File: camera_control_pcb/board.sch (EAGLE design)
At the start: 17 parts, among them Q1 MPSA42

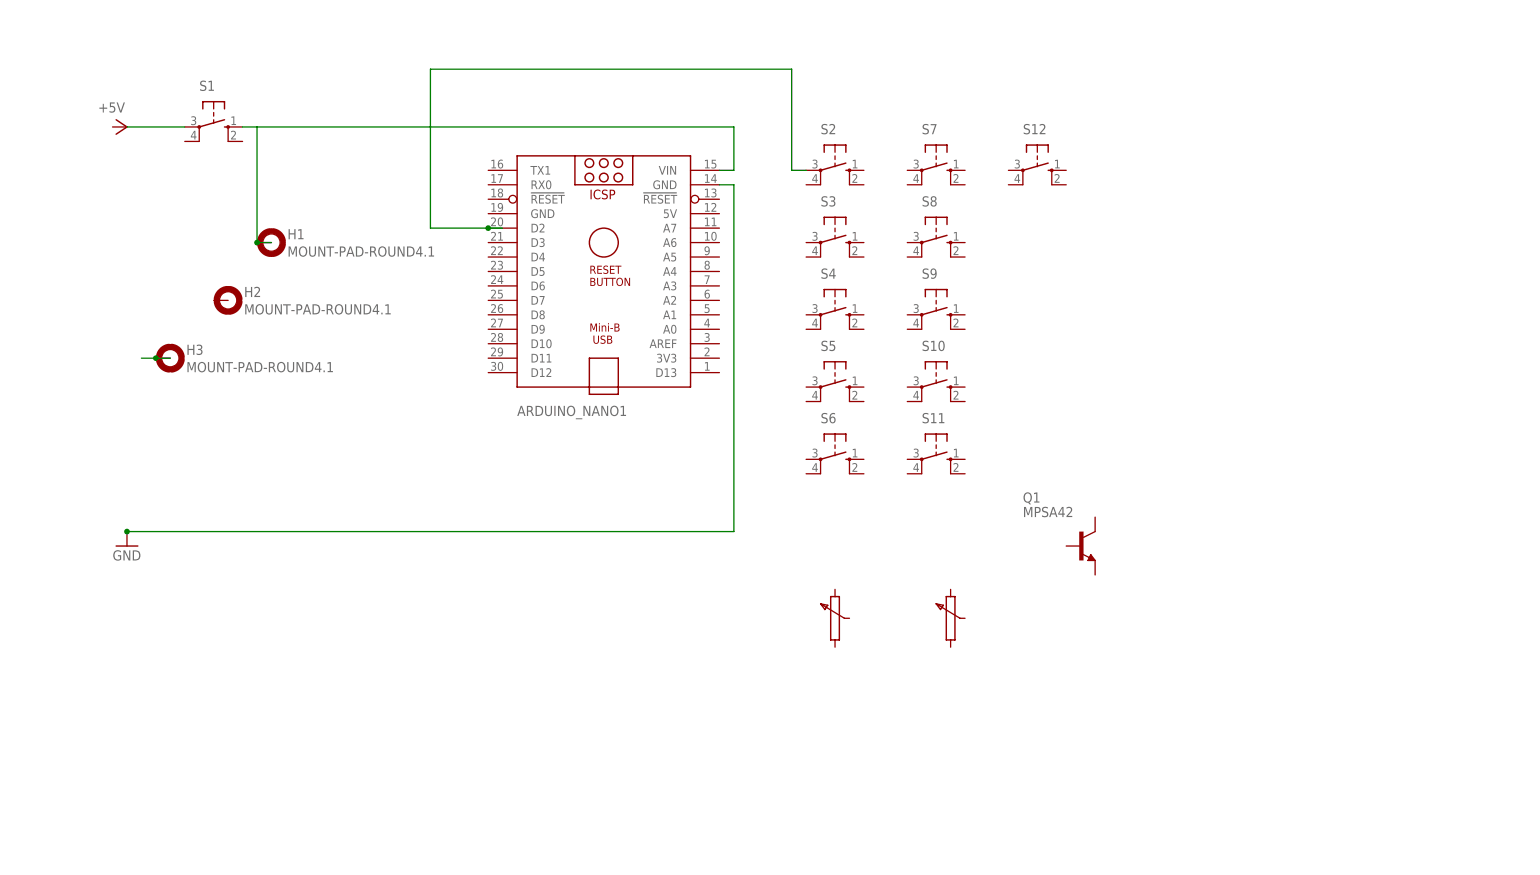
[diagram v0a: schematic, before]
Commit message: Rest of switch pins; demo board layout
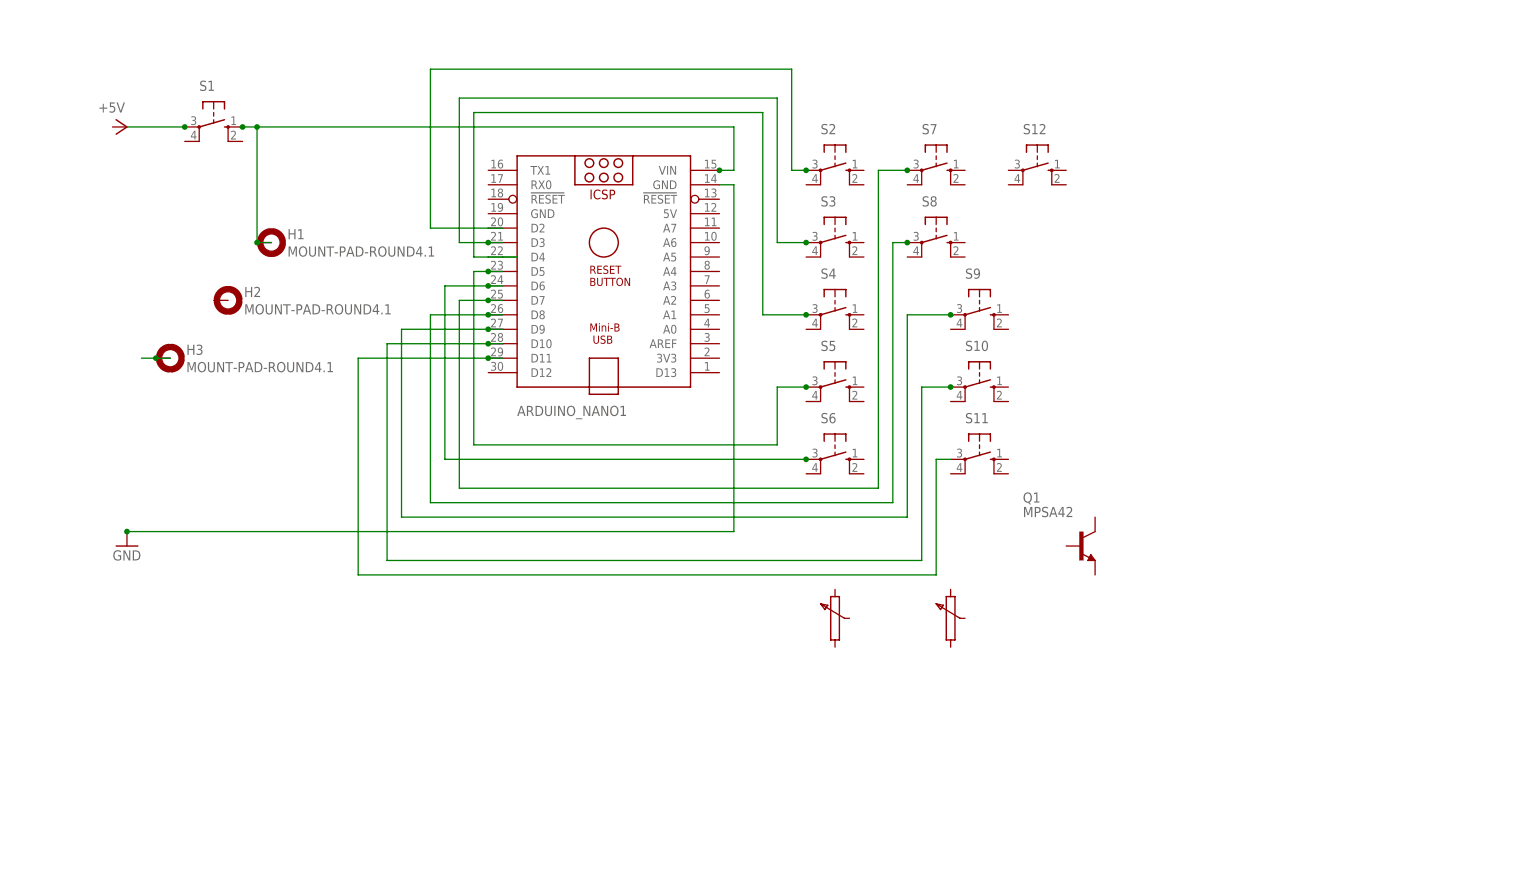
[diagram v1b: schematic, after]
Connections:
- new net N$10: ARDUINO_NANO1.D9, S9.P
- new net N$11: ARDUINO_NANO1.D10, S10.P
- new net N$12: ARDUINO_NANO1.D11, S11.P
- new net N$14: ARDUINO_NANO1.D4, S4.P
- new net N$5: ARDUINO_NANO1.D3, S3.P
- new net N$6: ARDUINO_NANO1.D7, S7.P
- new net N$7: ARDUINO_NANO1.D5, S5.P
- new net N$8: ARDUINO_NANO1.D6, S6.P
- new net N$9: ARDUINO_NANO1.D8, S8.P
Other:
- moved on the sheet: S10, S11, S9
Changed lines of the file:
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@@
 <attribute name="VALUE" x="104.775" y="72.39" size="1.778" layer="96"/>
 </instance>
-<instance part="S9" gate="1" x="101.6" y="55.88" smashed="yes" rot="R270">
-<attribute name="NAME" x="99.06" y="62.23" size="1.778" layer="95"/>
-<attribute name="VALUE" x="104.775" y="59.69" size="1.778" layer="96"/>
-</instance>
-<instance part="S10" gate="1" x="101.6" y="43.18" smashed="yes" rot="R270">
-<attribute name="NAME" x="99.06" y="49.53" size="1.778" layer="95"/>
-<attribute name="VALUE" x="104.775" y="46.99" size="1.778" layer="96"/>
-</instance>
-<instance part="S11" gate="1" x="101.6" y="30.48" smashed="yes" rot="R270">
-<attribute name="NAME" x="99.06" y="36.83" size="1.778" layer="95"/>
-<attribute name="VALUE" x="104.775" y="34.29" size="1.778" layer="96"/>
+<instance part="S9" gate="1" x="109.22" y="55.88" smashed="yes" rot="R270">
+<attribute name="NAME" x="106.68" y="62.23" size="1.778" layer="95"/>
+<attribute name="VALUE" x="112.395" y="59.69" size="1.778" layer="96"/>
+</instance>
+<instance part="S10" gate="1" x="109.22" y="43.18" smashed="yes" rot="R270">
+<attribute name="NAME" x="106.68" y="49.53" size="1.778" layer="95"/>
+<attribute name="VALUE" x="112.395" y="46.99" size="1.778" layer="96"/>
+</instance>
+<instance part="S11" gate="1" x="109.22" y="30.48" smashed="yes" rot="R270">
+<attribute name="NAME" x="106.68" y="36.83" size="1.778" layer="95"/>
+<attribute name="VALUE" x="112.395" y="34.29" size="1.778" layer="96"/>
 </instance>
 <instance part="S12" gate="1" x="119.38" y="81.28" smashed="yes" rot="R270">
@@
 <pinref part="S1" gate="1" pin="P"/>
 <wire x1="-40.64" y1="88.9" x2="-30.48" y2="88.9" width="0.1524" layer="91"/>
+<junction x="-30.48" y="88.9"/>
 </segment>
 </net>
@@
 <pinref part="H1" gate="G$1" pin="MOUNT"/>
 <junction x="-17.78" y="68.58"/>
+<junction x="-17.78" y="88.9"/>
+<junction x="63.5" y="81.28"/>
+<junction x="-20.32" y="88.9"/>
 </segment>
 </net>
@@
 <net name="N$5" class="0">
 <segment>
+<wire x1="25.4" y1="68.58" x2="22.86" y2="68.58" width="0.1524" layer="91"/>
+<wire x1="22.86" y1="68.58" x2="17.78" y2="68.58" width="0.1524" layer="91"/>
+<wire x1="17.78" y1="68.58" x2="17.78" y2="93.98" width="0.1524" layer="91"/>
+<wire x1="17.78" y1="93.98" x2="73.66" y2="93.98" width="0.1524" layer="91"/>
+<wire x1="73.66" y1="93.98" x2="73.66" y2="68.58" width="0.1524" layer="91"/>
+<pinref part="S3" gate="1" pin="P"/>
+<wire x1="73.66" y1="68.58" x2="78.74" y2="68.58" width="0.1524" layer="91"/>
+<pinref part="ARDUINO_NANO1" gate="G$1" pin="D3"/>
+<junction x="22.86" y="68.58"/>
+<junction x="78.74" y="68.58"/>
+</segment>
+</net>
+<net name="N$7" class="0">
+<segment>
+<pinref part="S5" gate="1" pin="P"/>
+<wire x1="78.74" y1="43.18" x2="73.66" y2="43.18" width="0.1524" layer="91"/>
+<wire x1="73.66" y1="43.18" x2="73.66" y2="33.02" width="0.1524" layer="91"/>
+<wire x1="73.66" y1="33.02" x2="20.32" y2="33.02" width="0.1524" layer="91"/>
+<wire x1="20.32" y1="33.02" x2="20.32" y2="63.5" width="0.1524" layer="91"/>
+<wire x1="20.32" y1="63.5" x2="22.86" y2="63.5" width="0.1524" layer="91"/>
+<pinref part="ARDUINO_NANO1" gate="G$1" pin="D5"/>
+<wire x1="22.86" y1="63.5" x2="25.4" y2="63.5" width="0.1524" layer="91"/>
+<junction x="22.86" y="63.5"/>
+<junction x="78.74" y="43.18"/>
+</segment>
+</net>
+<net name="N$8" class="0">
+<segment>
+<pinref part="S6" gate="1" pin="P"/>
+<wire x1="78.74" y1="30.48" x2="15.24" y2="30.48" width="0.1524" layer="91"/>
+<wire x1="15.24" y1="30.48" x2="15.24" y2="60.96" width="0.1524" layer="91"/>
+<wire x1="15.24" y1="60.96" x2="22.86" y2="60.96" width="0.1524" layer="91"/>
+<pinref part="ARDUINO_NANO1" gate="G$1" pin="D6"/>
+<wire x1="22.86" y1="60.96" x2="25.4" y2="60.96" width="0.1524" layer="91"/>
+<junction x="22.86" y="60.96"/>
+<junction x="78.74" y="30.48"/>
+</segment>
+</net>
+<net name="N$6" class="0">
+<segment>
+<pinref part="S7" gate="1" pin="P"/>
+<wire x1="96.52" y1="81.28" x2="91.44" y2="81.28" width="0.1524" layer="91"/>
+<wire x1="91.44" y1="81.28" x2="91.44" y2="25.4" width="0.1524" layer="91"/>
+<wire x1="91.44" y1="25.4" x2="17.78" y2="25.4" width="0.1524" layer="91"/>
+<wire x1="17.78" y1="25.4" x2="17.78" y2="58.42" width="0.1524" layer="91"/>
+<wire x1="17.78" y1="58.42" x2="22.86" y2="58.42" width="0.1524" layer="91"/>
+<pinref part="ARDUINO_NANO1" gate="G$1" pin="D7"/>
+<wire x1="22.86" y1="58.42" x2="25.4" y2="58.42" width="0.1524" layer="91"/>
+<junction x="22.86" y="58.42"/>
+<junction x="96.52" y="81.28"/>
+</segment>
+</net>
+<net name="N$9" class="0">
+<segment>
+<pinref part="S8" gate="1" pin="P"/>
+<wire x1="96.52" y1="68.58" x2="93.98" y2="68.58" width="0.1524" layer="91"/>
+<wire x1="93.98" y1="68.58" x2="93.98" y2="22.86" width="0.1524" layer="91"/>
+<wire x1="93.98" y1="22.86" x2="12.7" y2="22.86" width="0.1524" layer="91"/>
+<wire x1="12.7" y1="22.86" x2="12.7" y2="55.88" width="0.1524" layer="91"/>
+<wire x1="12.7" y1="55.88" x2="22.86" y2="55.88" width="0.1524" layer="91"/>
+<pinref part="ARDUINO_NANO1" gate="G$1" pin="D8"/>
+<wire x1="22.86" y1="55.88" x2="25.4" y2="55.88" width="0.1524" layer="91"/>
+<junction x="22.86" y="55.88"/>
+<junction x="96.52" y="68.58"/>
+</segment>
+</net>
+<net name="N$10" class="0">
+<segment>
+<pinref part="S9" gate="1" pin="P"/>
+<wire x1="104.14" y1="55.88" x2="96.52" y2="55.88" width="0.1524" layer="91"/>
+<wire x1="96.52" y1="55.88" x2="96.52" y2="20.32" width="0.1524" layer="91"/>
+<wire x1="96.52" y1="20.32" x2="7.62" y2="20.32" width="0.1524" layer="91"/>
+<wire x1="7.62" y1="20.32" x2="7.62" y2="53.34" width="0.1524" layer="91"/>
+<wire x1="7.62" y1="53.34" x2="22.86" y2="53.34" width="0.1524" layer="91"/>
+<pinref part="ARDUINO_NANO1" gate="G$1" pin="D9"/>
+<junction x="22.86" y="53.34"/>
+<wire x1="22.86" y1="53.34" x2="25.4" y2="53.34" width="0.1524" layer="91"/>
+<junction x="104.14" y="55.88"/>
+</segment>
+</net>
+<net name="N$11" class="0">
+<segment>
+<pinref part="S10" gate="1" pin="P"/>
+<wire x1="104.14" y1="43.18" x2="99.06" y2="43.18" width="0.1524" layer="91"/>
+<wire x1="99.06" y1="43.18" x2="99.06" y2="12.7" width="0.1524" layer="91"/>
+<wire x1="99.06" y1="12.7" x2="5.08" y2="12.7" width="0.1524" layer="91"/>
+<wire x1="5.08" y1="12.7" x2="5.08" y2="50.8" width="0.1524" layer="91"/>
+<wire x1="5.08" y1="50.8" x2="22.86" y2="50.8" width="0.1524" layer="91"/>
+<pinref part="ARDUINO_NANO1" gate="G$1" pin="D10"/>
+<junction x="22.86" y="50.8"/>
+<wire x1="22.86" y1="50.8" x2="25.4" y2="50.8" width="0.1524" layer="91"/>
+<junction x="104.14" y="43.18"/>
+</segment>
+</net>
+<net name="N$12" class="0">
+<segment>
+<pinref part="S11" gate="1" pin="P"/>
+<wire x1="104.14" y1="30.48" x2="101.6" y2="30.48" width="0.1524" layer="91"/>
+<wire x1="101.6" y1="30.48" x2="101.6" y2="10.16" width="0.1524" layer="91"/>
+<wire x1="101.6" y1="10.16" x2="0" y2="10.16" width="0.1524" layer="91"/>
+<wire x1="0" y1="10.16" x2="0" y2="48.26" width="0.1524" layer="91"/>
+<wire x1="0" y1="48.26" x2="22.86" y2="48.26" width="0.1524" layer="91"/>
+<pinref part="ARDUINO_NANO1" gate="G$1" pin="D11"/>
+<junction x="22.86" y="48.26"/>
+<wire x1="22.86" y1="48.26" x2="25.4" y2="48.26" width="0.1524" layer="91"/>
+</segment>
+</net>
+<net name="N$13" class="0">
+<segment>
+<pinref part="S2" gate="1" pin="P"/>
+<junction x="78.74" y="81.28"/>
+<wire x1="76.2" y1="81.28" x2="78.74" y2="81.28" width="0.1524" layer="91"/>
+<wire x1="76.2" y1="99.06" x2="76.2" y2="81.28" width="0.1524" layer="91"/>
+<wire x1="12.7" y1="99.06" x2="76.2" y2="99.06" width="0.1524" layer="91"/>
+<wire x1="12.7" y1="71.12" x2="12.7" y2="99.06" width="0.1524" layer="91"/>
 <wire x1="25.4" y1="71.12" x2="22.86" y2="71.12" width="0.1524" layer="91"/>
-<wire x1="22.86" y1="71.12" x2="12.7" y2="71.12" width="0.1524" layer="91"/>
-<wire x1="12.7" y1="71.12" x2="12.7" y2="99.06" width="0.1524" layer="91"/>
-<wire x1="12.7" y1="99.06" x2="76.2" y2="99.06" width="0.1524" layer="91"/>
-<pinref part="S2" gate="1" pin="P"/>
-<wire x1="76.2" y1="99.06" x2="76.2" y2="81.28" width="0.1524" layer="91"/>
-<wire x1="76.2" y1="81.28" x2="78.74" y2="81.28" width="0.1524" layer="91"/>
 <pinref part="ARDUINO_NANO1" gate="G$1" pin="D2"/>
-<junction x="22.86" y="71.12"/>
-</segment>
-</net>
+<wire x1="12.7" y1="71.12" x2="22.86" y2="71.12" width="0.1524" layer="91"/>
+</segment>
+</net>
+<net name="N$14" class="0">
+<segment>
+<pinref part="S4" gate="1" pin="P"/>
+<junction x="78.74" y="55.88"/>
+<wire x1="78.74" y1="55.88" x2="71.12" y2="55.88" width="0.1524" layer="91"/>
+<wire x1="71.12" y1="55.88" x2="71.12" y2="91.44" width="0.1524" layer="91"/>
+<wire x1="71.12" y1="91.44" x2="20.32" y2="91.44" width="0.1524" layer="91"/>
+<wire x1="20.32" y1="91.44" x2="20.32" y2="66.04" width="0.1524" layer="91"/>
+<pinref part="ARDUINO_NANO1" gate="G$1" pin="D4"/>
+<wire x1="22.86" y1="66.04" x2="25.4" y2="66.04" width="0.1524" layer="91"/>
+<wire x1="25.4" y1="66.04" x2="27.94" y2="66.04" width="0.1524" layer="91"/>
+<wire x1="20.32" y1="66.04" x2="22.86" y2="66.04" width="0.1524" layer="91"/>
+</segment>
+</net>

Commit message: Finished placing components
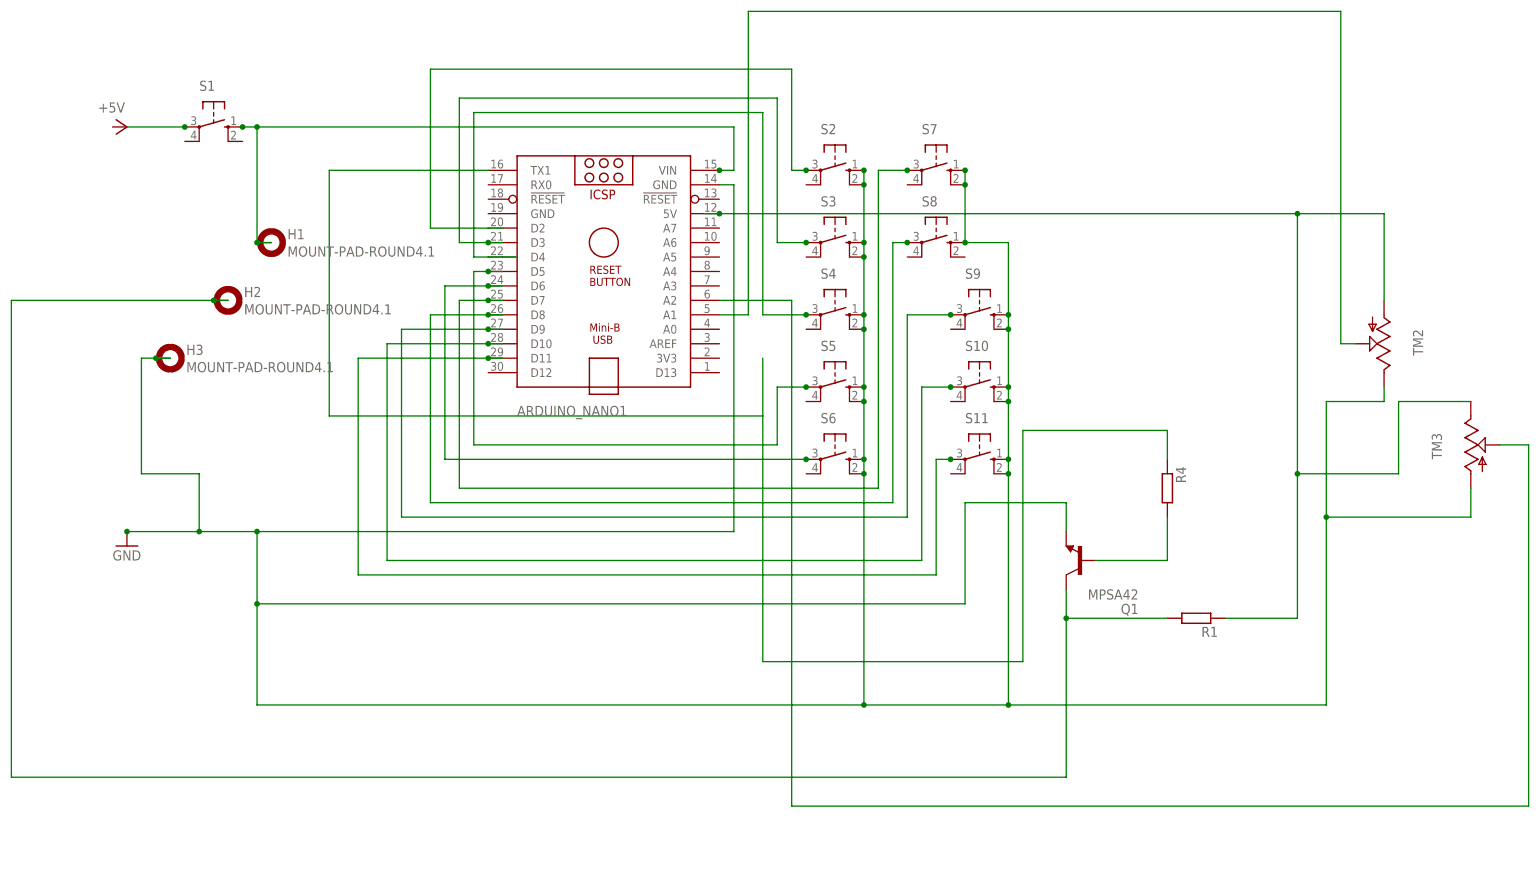
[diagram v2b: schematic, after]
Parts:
- removed S12: (no value), switch-omron:40-XX
- added R1, R4: (no value), rcl:R-EU_0204/2V
- added TM2, TM3: (no value), Bourns PTA series:TRIMSLIDE75
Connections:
- new net N$15: ARDUINO_NANO1.TX1, R4.1
- new net N$16: H2.MOUNT, Q1.C, R1.2
- new net N$17: ARDUINO_NANO1.5V, R1.1, TM2.A, TM3.B
- new net N$18: ARDUINO_NANO1.A1, TM2.WIPER
- new net N$19: ARDUINO_NANO1.A2, TM3.WIPER
- net N$3: now also H3.MOUNT, Q1.E, S10.S, S10.S1, S11.S, S11.S1, S2.S, S2.S1, S3.S, S3.S1, S4.S, S4.S1, S5.S, S5.S1, S6.S, S6.S1, S7.S, S7.S1, S8.S, S9.S, S9.S1, TM2.B, TM3.A
- net N$4: now also Q1.B, R4.2; no longer H3.MOUNT
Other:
- moved on the sheet: Q1
